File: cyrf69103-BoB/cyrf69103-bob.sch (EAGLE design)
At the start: 32 parts

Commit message: Added revision and author
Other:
- note added: "Joseph Moreland"
- note added: "v0.1"
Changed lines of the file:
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@@
 Load Capacitance 10pF
 </text>
+<text x="177.8" y="7.62" size="2.54" layer="97">Joseph Moreland</text>
+<text x="236.22" y="7.62" size="2.54" layer="97">v0.1</text>
 </plain>
 <instances>

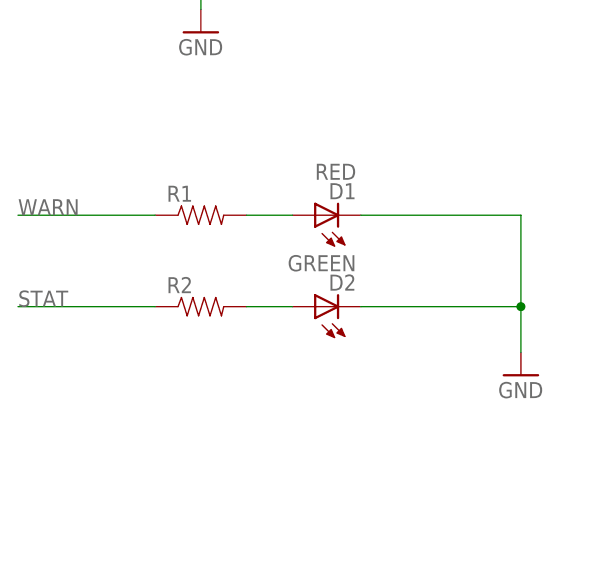
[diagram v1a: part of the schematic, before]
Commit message: Screwed up that last commit.  this update include changes to the production gerber folders.  Adds hackvana to the cyrf6936-BoB and cleans up the fab notes a bit.  Still need to standardize and parameterize the creation of the gerbers.
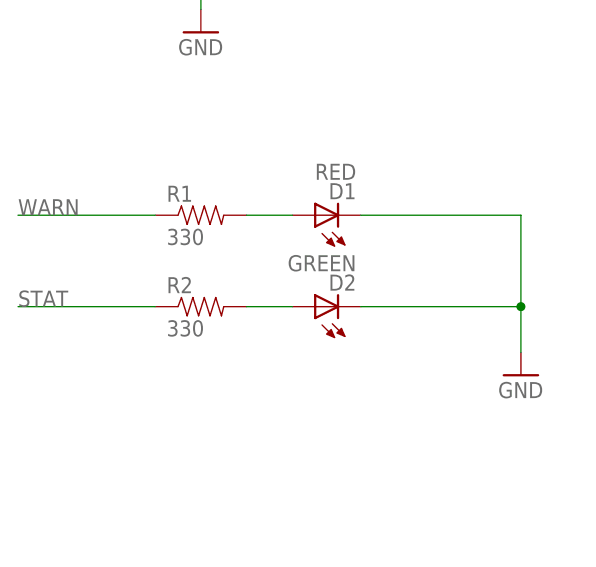
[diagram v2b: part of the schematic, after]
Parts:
- D1: PARTNO (none) -> LTST-C191TBKT
- D2: PARTNO (none) -> LTST-C190KGKT
- R1, R2: value (none) -> 330; PARTNO (none) -> CRCW0402330RJNED
- U$1: PARTNO (none) -> CYRF69103-40LFXC
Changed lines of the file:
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@@
 <part name="IRQ" library="JCM" deviceset="SOLDER_PAD" device=""/>
 <part name="GND" library="JCM" deviceset="SOLDER_PAD" device=""/>
-<part name="U$1" library="JCM" deviceset="CYRF69103" device=""/>
+<part name="U$1" library="JCM" deviceset="CYRF69103" device="">
+<attribute name="PARTNO" value="CYRF69103-40LFXC"/>
+</part>
 <part name="C2" library="SparkFun-Passives" deviceset="CAP" device="0402-CAP" value="0.47uF">
 <attribute name="PARTNO" value="GRM155R60J474KE19D"/>
@@
 <part name="SDATA" library="JCM" deviceset="SOLDER_PAD" device=""/>
 <part name="VCC_JMP" library="JCM" deviceset="SOLDER_PAD" device=""/>
-<part name="D2" library="SparkFun-LED" deviceset="LED-GREEN" device="0603" value="GREEN"/>
-<part name="D1" library="SparkFun-LED" deviceset="LED-RED" device="0603" value="RED"/>
+<part name="D2" library="SparkFun-LED" deviceset="LED-GREEN" device="0603" value="GREEN">
+<attribute name="PARTNO" value="LTST-C190KGKT"/>
+</part>
+<part name="D1" library="SparkFun-LED" deviceset="LED-RED" device="0603" value="RED">
+<attribute name="PARTNO" value="LTST-C191TBKT"/>
+</part>
 <part name="GND12" library="SparkFun-Aesthetics" deviceset="GND" device=""/>
-<part name="R1" library="SparkFun-Passives" deviceset="RESISTOR" device="0402-RES"/>
-<part name="R2" library="SparkFun-Passives" deviceset="RESISTOR" device="0402-RES"/>
+<part name="R1" library="SparkFun-Passives" deviceset="RESISTOR" device="0402-RES" value="330">
+<attribute name="PARTNO" value="CRCW0402330RJNED"/>
+</part>
+<part name="R2" library="SparkFun-Passives" deviceset="RESISTOR" device="0402-RES" value="330">
+<attribute name="PARTNO" value="CRCW0402330RJNED"/>
+</part>
 </parts>
 <sheets>
@@
 <attribute name="NAME" x="27.686" y="91.186" size="1.778" layer="95" rot="R180"/>
 </instance>
-<instance part="U$1" gate="G$1" x="104.14" y="83.82"/>
+<instance part="U$1" gate="G$1" x="104.14" y="83.82">
+<attribute name="PARTNO" x="104.14" y="83.82" size="1.778" layer="96" display="off"/>
+</instance>
 <instance part="C2" gate="G$1" x="134.62" y="132.08" rot="R90">
 <attribute name="PARTNO" x="134.62" y="132.08" size="1.778" layer="96" rot="R90" display="off"/>
@@
 <attribute name="NAME" x="147.574" y="172.974" size="1.778" layer="95"/>
 </instance>
-<instance part="D2" gate="G$1" x="50.8" y="33.02" rot="R90"/>
-<instance part="D1" gate="G$1" x="50.8" y="43.18" rot="R90"/>
+<instance part="D2" gate="G$1" x="50.8" y="33.02" rot="R90">
+<attribute name="PARTNO" x="50.8" y="33.02" size="1.778" layer="96" display="off"/>
+</instance>
+<instance part="D1" gate="G$1" x="50.8" y="43.18" rot="R90">
+<attribute name="PARTNO" x="50.8" y="43.18" size="1.778" layer="96" display="off"/>
+</instance>
 <instance part="GND12" gate="1" x="73.66" y="25.4"/>
-<instance part="R1" gate="G$1" x="38.1" y="43.18"/>
-<instance part="R2" gate="G$1" x="38.1" y="33.02"/>
+<instance part="R1" gate="G$1" x="38.1" y="43.18">
+<attribute name="PARTNO" x="38.1" y="43.18" size="1.778" layer="96" display="off"/>
+</instance>
+<instance part="R2" gate="G$1" x="38.1" y="33.02">
+<attribute name="PARTNO" x="38.1" y="33.02" size="1.778" layer="96" display="off"/>
+</instance>
 </instances>
 <busses>
